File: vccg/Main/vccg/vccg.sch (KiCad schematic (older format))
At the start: 47 parts, among them J1 MelodyClock, J10 melody, J11 oled, J2 ChordClock, J3 ChordCV, J4 OctaveCV, J5 MelodyCV, J6 Conn_02x05_Odd_Even, J7 root, J8 chord1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

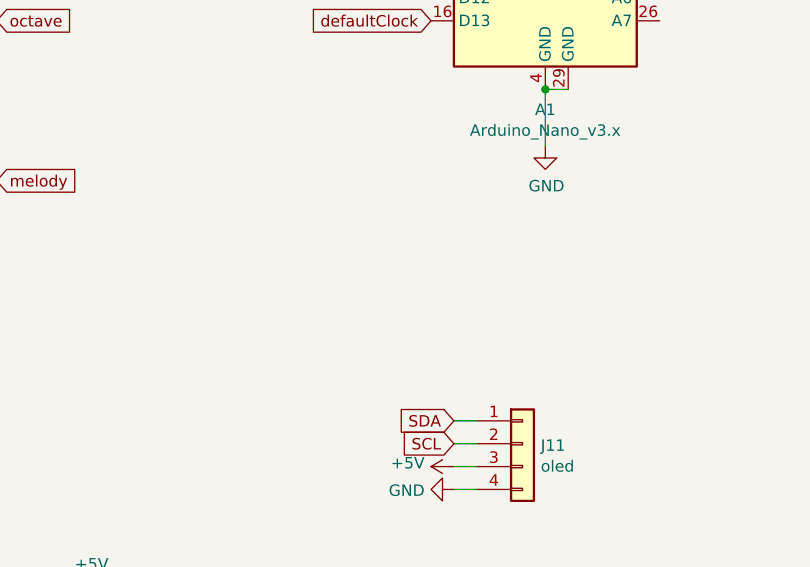
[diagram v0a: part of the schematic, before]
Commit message: add ic2 pull up resistors. Rewire to 10HP.
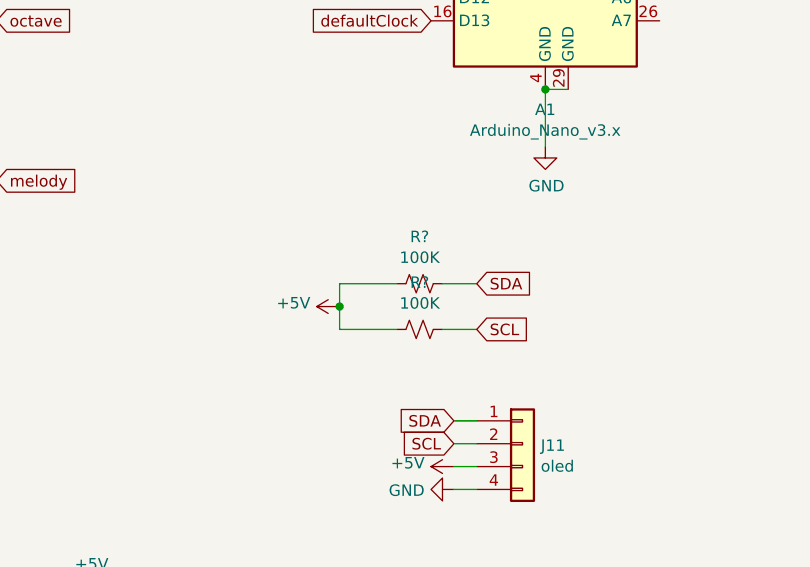
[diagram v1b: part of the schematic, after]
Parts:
- added R? (x2): 100K, Resistor_THT:R_Axial_DIN0207_L6.3mm_D2.5mm_P7.62mm_Horizontal, symbol Device:R_Small_US
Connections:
- net +5V: now also R?.2, R?.2
- net SCL: now also R?.1
- net SDA: now also R?.1
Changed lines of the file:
@@
 Wire Wire Line
 	4550 4250 4650 4250
+$Comp
+L Device:R_Small_US R?
+U 1 1 61B1FA80
+P 4400 3650
+F 0 "R?" V 4195 3650 50  0000 C CNN
+F 1 "100K" V 4286 3650 50  0000 C CNN
+F 2 "Resistor_THT:R_Axial_DIN0207_L6.3mm_D2.5mm_P7.62mm_Horizontal" H 4400 3650 50  0001 C CNN
+F 3 "~" H 4400 3650 50  0001 C CNN
+	1    4400 3650
+	0    1    1    0
+$EndComp
+$Comp
+L Device:R_Small_US R?
+U 1 1 61B20B5F
+P 4400 3850
+F 0 "R?" V 4195 3850 50  0000 C CNN
+F 1 "100K" V 4286 3850 50  0000 C CNN
+F 2 "Resistor_THT:R_Axial_DIN0207_L6.3mm_D2.5mm_P7.62mm_Horizontal" H 4400 3850 50  0001 C CNN
+F 3 "~" H 4400 3850 50  0001 C CNN
+	1    4400 3850
+	0    1    1    0
+$EndComp
+Text GLabel 4650 3650 2    50   Input ~ 0
+SDA
+Text GLabel 4650 3850 2    50   Input ~ 0
+SCL
+$Comp
+L power:+5V #PWR?
+U 1 1 61B236AE
+P 4050 3750
+F 0 "#PWR?" H 4050 3600 50  0001 C CNN
+F 1 "+5V" V 4065 3878 50  0000 L CNN
+F 2 "" H 4050 3750 50  0001 C CNN
+F 3 "" H 4050 3750 50  0001 C CNN
+	1    4050 3750
+	0    -1   -1   0
+$EndComp
+Wire Wire Line
+	4050 3750 4050 3650
+Wire Wire Line
+	4050 3650 4300 3650
+Wire Wire Line
+	4300 3850 4050 3850
+Wire Wire Line
+	4050 3850 4050 3750
+Connection ~ 4050 3750
+Wire Wire Line
+	4500 3650 4650 3650
+Wire Wire Line
+	4500 3850 4650 3850
 $EndSCHEMATC

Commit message: Yeet all them grb files into place
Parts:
- gave numbers to parts that had none: 2
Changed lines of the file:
@@
 	4550 4250 4650 4250
 $Comp
-L Device:R_Small_US R?
+L Device:R_Small_US R18
 U 1 1 61B1FA80
 P 4400 3650
-F 0 "R?" V 4195 3650 50  0000 C CNN
+F 0 "R18" V 4195 3650 50  0000 C CNN
 F 1 "100K" V 4286 3650 50  0000 C CNN
 F 2 "Resistor_THT:R_Axial_DIN0207_L6.3mm_D2.5mm_P7.62mm_Horizontal" H 4400 3650 50  0001 C CNN
@@
 $EndComp
 $Comp
-L Device:R_Small_US R?
+L Device:R_Small_US R19
 U 1 1 61B20B5F
 P 4400 3850
-F 0 "R?" V 4195 3850 50  0000 C CNN
+F 0 "R19" V 4195 3850 50  0000 C CNN
 F 1 "100K" V 4286 3850 50  0000 C CNN
 F 2 "Resistor_THT:R_Axial_DIN0207_L6.3mm_D2.5mm_P7.62mm_Horizontal" H 4400 3850 50  0001 C CNN
@@
 SCL
 $Comp
-L power:+5V #PWR?
+L power:+5V #PWR0136
 U 1 1 61B236AE
 P 4050 3750
-F 0 "#PWR?" H 4050 3600 50  0001 C CNN
+F 0 "#PWR0136" H 4050 3600 50  0001 C CNN
 F 1 "+5V" V 4065 3878 50  0000 L CNN
 F 2 "" H 4050 3750 50  0001 C CNN

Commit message: vccg updates and gbrs and stuff
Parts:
- removed R3, R4, R5: 100K, Resistor_THT:R_Axial_DIN0207_L6.3mm_D2.5mm_P7.62mm_Horizontal, symbol Device:R_Small_US
- removed U4: TL074, Package_SO:TSSOP-14_4.4x5mm_P0.65mm, symbol Amplifier_Operational:TL074
- C1, C2, C5: footprint Capacitor_THT:C_Disc_D7.5mm_W5.0mm_P7.50mm -> Capacitor_THT:C_Disc_D4.3mm_W1.9mm_P5.00mm
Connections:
- net chord1: now also R9.2
- net chord2: now also R10.2
- net quant: now also R11.2
- net root: now also R8.2
- net at U1.3 (+): now also RV1.2
- net at U1.5 (+): now also RV2.2
- net at U1.10 (+): now also J5.T
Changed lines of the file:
@@
-$EndComp
-$Comp
-L Amplifier_Operational:TL074 U4
-U 1 1 6147B30E
-P 8850 1700
-F 0 "U4" H 8850 2067 50  0000 C CNN
-F 1 "TL074" H 8850 1976 50  0000 C CNN
-F 2 "Package_SO:TSSOP-14_4.4x5mm_P0.65mm" H 8800 1800 50  0001 C CNN
-F 3 "http://www.ti.com/lit/ds/symlink/tl071.pdf" H 8900 1900 50  0001 C CNN
-	1    8850 1700
-	1    0    0    -1
-$EndComp
-$Comp
-L Amplifier_Operational:TL074 U4
-U 2 1 6147C57C
-P 8850 2450
-F 0 "U4" H 8850 2817 50  0000 C CNN
-F 1 "TL074" H 8850 2726 50  0000 C CNN
-F 2 "Package_SO:TSSOP-14_4.4x5mm_P0.65mm" H 8800 2550 50  0001 C CNN
-F 3 "http://www.ti.com/lit/ds/symlink/tl071.pdf" H 8900 2650 50  0001 C CNN
-	2    8850 2450
-	1    0    0    -1
-$EndComp
-$Comp
-L Amplifier_Operational:TL074 U4
-U 3 1 6147D772
-P 8900 3250
-F 0 "U4" H 8900 3617 50  0000 C CNN
-F 1 "TL074" H 8900 3526 50  0000 C CNN
-F 2 "Package_SO:TSSOP-14_4.4x5mm_P0.65mm" H 8850 3350 50  0001 C CNN
-F 3 "http://www.ti.com/lit/ds/symlink/tl071.pdf" H 8950 3450 50  0001 C CNN
-	3    8900 3250
-	1    0    0    -1
-$EndComp
-$Comp
-L Amplifier_Operational:TL074 U4
-U 4 1 6147E4EE
-P 8900 3900
-F 0 "U4" H 8900 4267 50  0000 C CNN
-F 1 "TL074" H 8900 4176 50  0000 C CNN
-F 2 "Package_SO:TSSOP-14_4.4x5mm_P0.65mm" H 8850 4000 50  0001 C CNN
-F 3 "http://www.ti.com/lit/ds/symlink/tl071.pdf" H 8950 4100 50  0001 C CNN
-	4    8900 3900
-	1    0    0    -1
-$EndComp
-$Comp
-L Amplifier_Operational:TL074 U4
-U 5 1 6147F980
-P 8850 1700
-F 0 "U4" H 8808 1746 50  0000 L CNN
-F 1 "TL074" H 8808 1655 50  0000 L CNN
-F 2 "Package_SO:TSSOP-14_4.4x5mm_P0.65mm" H 8800 1800 50  0001 C CNN
-F 3 "http://www.ti.com/lit/ds/symlink/tl071.pdf" H 8900 1900 50  0001 C CNN
-	5    8850 1700
-	1    0    0    -1
 $EndComp
 $Comp
@@
 F 0 "C2" H 4342 7096 50  0000 L CNN
 F 1 "10n" H 4342 7005 50  0000 L CNN
-F 2 "Capacitor_THT:C_Disc_D7.5mm_W5.0mm_P7.50mm" H 4250 7050 50  0001 C CNN
+F 2 "Capacitor_THT:C_Disc_D4.3mm_W1.9mm_P5.00mm" H 4250 7050 50  0001 C CNN
 F 3 "~" H 4250 7050 50  0001 C CNN
 	1    4250 7050
@@
 F 0 "C1" H 4342 6796 50  0000 L CNN
 F 1 "10n" H 4342 6705 50  0000 L CNN
-F 2 "Capacitor_THT:C_Disc_D7.5mm_W5.0mm_P7.50mm" H 4250 6750 50  0001 C CNN
+F 2 "Capacitor_THT:C_Disc_D4.3mm_W1.9mm_P5.00mm" H 4250 6750 50  0001 C CNN
 F 3 "~" H 4250 6750 50  0001 C CNN
 	1    4250 6750
@@
 F 0 "C5" H 5892 7046 50  0000 L CNN
 F 1 "10n" H 5892 6955 50  0000 L CNN
-F 2 "Capacitor_THT:C_Disc_D7.5mm_W5.0mm_P7.50mm" H 5800 7000 50  0001 C CNN
+F 2 "Capacitor_THT:C_Disc_D4.3mm_W1.9mm_P5.00mm" H 5800 7000 50  0001 C CNN
 F 3 "~" H 5800 7000 50  0001 C CNN
 	1    5800 7000
@@
 Wire Wire Line
 	2150 1350 2150 1450
-$Comp
-L Device:R_Small_US R3
-U 1 1 6152661D
-P 1550 1650
-F 0 "R3" V 1345 1650 50  0000 C CNN
-F 1 "100K" V 1436 1650 50  0000 C CNN
-F 2 "Resistor_THT:R_Axial_DIN0207_L6.3mm_D2.5mm_P7.62mm_Horizontal" H 1550 1650 50  0001 C CNN
-F 3 "~" H 1550 1650 50  0001 C CNN
-	1    1550 1650
-	0    1    1    0
-$EndComp
-$Comp
-L Device:R_Small_US R4
-U 1 1 615276A2
-P 1600 2400
-F 0 "R4" V 1395 2400 50  0000 C CNN
-F 1 "100K" V 1486 2400 50  0000 C CNN
-F 2 "Resistor_THT:R_Axial_DIN0207_L6.3mm_D2.5mm_P7.62mm_Horizontal" H 1600 2400 50  0001 C CNN
-F 3 "~" H 1600 2400 50  0001 C CNN
-	1    1600 2400
-	0    1    1    0
-$EndComp
-$Comp
-L Device:R_Small_US R5
-U 1 1 61527E2C
-P 1600 3100
-F 0 "R5" V 1395 3100 50  0000 C CNN
-F 1 "100K" V 1486 3100 50  0000 C CNN
-F 2 "Resistor_THT:R_Axial_DIN0207_L6.3mm_D2.5mm_P7.62mm_Horizontal" H 1600 3100 50  0001 C CNN
-F 3 "~" H 1600 3100 50  0001 C CNN
-	1    1600 3100
-	0    1    1    0
-$EndComp
 $Comp
 L Connector:AudioJack2_SwitchT J7
@@
 Wire Wire Line
 	1500 2500 1500 2400
-Wire Wire Line
-	1700 2400 1950 2400
 $Comp
 L power:GND #PWR0116
@@
 	1400 1750 1400 1650
 Wire Wire Line
-	1400 1650 1450 1650
-Wire Wire Line
-	1650 1650 1950 1650
-Wire Wire Line
 	1950 1850 1850 1850
 Wire Wire Line
@@
 Wire Wire Line
 	2550 2750 2550 2500
-Wire Wire Line
-	1100 3100 1500 3100
-Wire Wire Line
-	1700 3100 1950 3100
 Wire Wire Line
 	1950 3300 1800 3300
@@
 Text GLabel 7700 5050 2    50   Input ~ 0
 quant
-Text GLabel 8600 3800 0    50   Input ~ 0
+Text GLabel 9100 3900 0    50   Input ~ 0
 quant
-Text GLabel 8600 3150 0    50   Input ~ 0
+Text GLabel 9100 3250 0    50   Input ~ 0
 chord2
-Text GLabel 8550 2350 0    50   Input ~ 0
+Text GLabel 9100 2450 0    50   Input ~ 0
 chord1
-Text GLabel 8550 1600 0    50   Input ~ 0
+Text GLabel 9050 1700 0    50   Input ~ 0
 root
 $Comp
@@
 	0    1    1    0
 $EndComp
-$Comp
-L power:+12V #PWR0122
-U 1 1 616AF12F
-P 8750 1300
-F 0 "#PWR0122" H 8750 1150 50  0001 C CNN
-F 1 "+12V" H 8765 1473 50  0000 C CNN
-F 2 "" H 8750 1300 50  0001 C CNN
-F 3 "" H 8750 1300 50  0001 C CNN
-	1    8750 1300
-	1    0    0    -1
-$EndComp
-$Comp
-L power:-12V #PWR0123
-U 1 1 616D2BDA
-P 8750 2050
-F 0 "#PWR0123" H 8750 2150 50  0001 C CNN
-F 1 "-12V" H 8765 2223 50  0000 C CNN
-F 2 "" H 8750 2050 50  0001 C CNN
-F 3 "" H 8750 2050 50  0001 C CNN
-	1    8750 2050
-	-1   0    0    1
-$EndComp
-Wire Wire Line
-	8750 1300 8750 1400
-Wire Wire Line
-	8750 2050 8750 2000
-Wire Wire Line
-	8550 1800 8550 2200
-Wire Wire Line
-	8550 2200 9150 2200
-Wire Wire Line
-	9150 2200 9150 1700
-Wire Wire Line
-	9150 1700 9450 1700
-Connection ~ 9150 1700
-Wire Wire Line
-	9150 2450 9400 2450
 Wire Wire Line
 	9650 2450 10000 2450
 Wire Wire Line
-	9200 3250 9400 3250
-Wire Wire Line
 	9700 3250 10000 3250
 Wire Wire Line
-	9200 3900 9400 3900
-Wire Wire Line
 	9700 3900 10000 3900
-Wire Wire Line
-	8600 4000 8600 4150
-Wire Wire Line
-	8600 4150 9400 4150
-Wire Wire Line
-	9400 4150 9400 3900
-Connection ~ 9400 3900
-Wire Wire Line
-	9400 3900 9500 3900
-Wire Wire Line
-	8600 3350 8600 3500
-Wire Wire Line
-	8600 3500 9400 3500
-Wire Wire Line
-	9400 3500 9400 3250
-Connection ~ 9400 3250
-Wire Wire Line
-	9400 3250 9500 3250
-Wire Wire Line
-	8550 2550 8550 2700
-Wire Wire Line
-	8550 2700 9400 2700
-Wire Wire Line
-	9400 2700 9400 2450
-Connection ~ 9400 2450
-Wire Wire Line
-	9400 2450 9450 2450
 Wire Wire Line
 	9650 1700 10000 1700
@@
 Wire Wire Line
 	4500 3850 4650 3850
+Wire Wire Line
+	9500 3900 9100 3900
+Wire Wire Line
+	9500 3250 9100 3250
+Wire Wire Line
+	9450 2450 9100 2450
+Wire Wire Line
+	9450 1700 9050 1700
+Wire Wire Line
+	1400 1650 1950 1650
+Wire Wire Line
+	1500 2400 1950 2400
+Wire Wire Line
+	1100 3100 1950 3100
 $EndSCHEMATC
